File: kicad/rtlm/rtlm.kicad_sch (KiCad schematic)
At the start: 261 parts, among them IC1 ESP32-S3FN8, IC2 TPS25940ARVCR, IC3 PE4259, IC4 TPS2553DBVR, IC5 TLV9004IDR, IC6 TLV9004IDR, IC7 TCAN1042HGVDR, IC8 TPS2553DBVR, IC9 TLC59116IPWR, J1 USB_C_Receptacle_USB2.0_16P, J10 TEMP_2, J11 TEMP_3, J12 TEMP_4, J13 ANALOG_1, J14 ANALOG_2, J15 ANALOG_3, J16 ANALOG_4, J17 DM3AT-SF-PEJM5, J18 CAN_EXPANSION, J19 BATTERY_VOLTAGE_SENSE_LINE, J2 Conn_01x02, J3 UART_DEBUG_3V3, J4 LORA_ANT, J5 PULSE_1, J6 PULSE_2, J7 PULSE_3, J8 PULSE_4, J9 TEMP_1, Q1 DMP2035U-7, SW1 SW_Push, SW2 SW_Push, U1 TPS62130A, U10 RV-3028-C7, U2 TPS2116DRL, U3 TPD2EUSB30, U4 SX1262IMLTRT, U5 SN74LVC14ADR, U6 MCP3208-BI/SL, U7 REF3025AIDBZR, U8 AMC3330, U9 ADS1115IDGS, Y1 40MHz, Y2 TG2520SMN 32.0000M-MCGNNM3

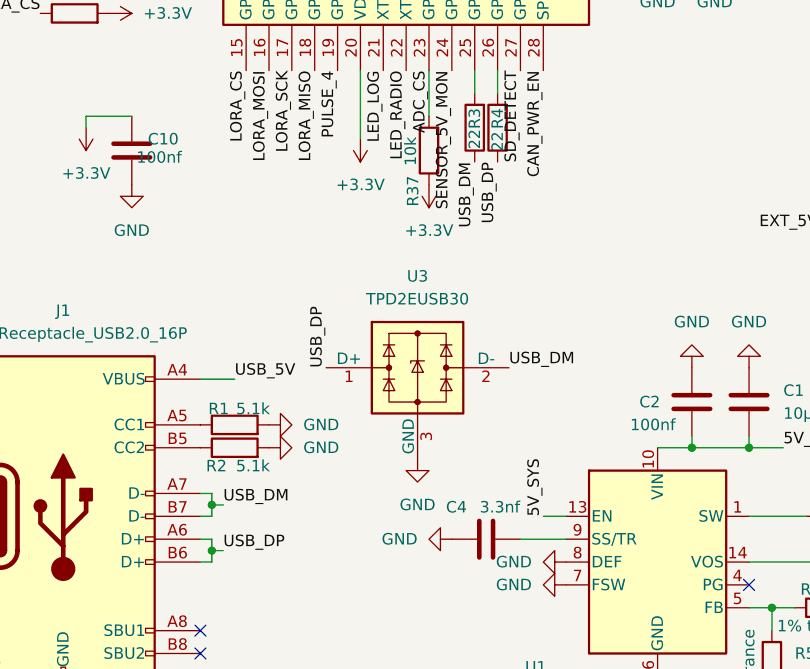
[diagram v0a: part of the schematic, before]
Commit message: feat: USB routing, thermal vias
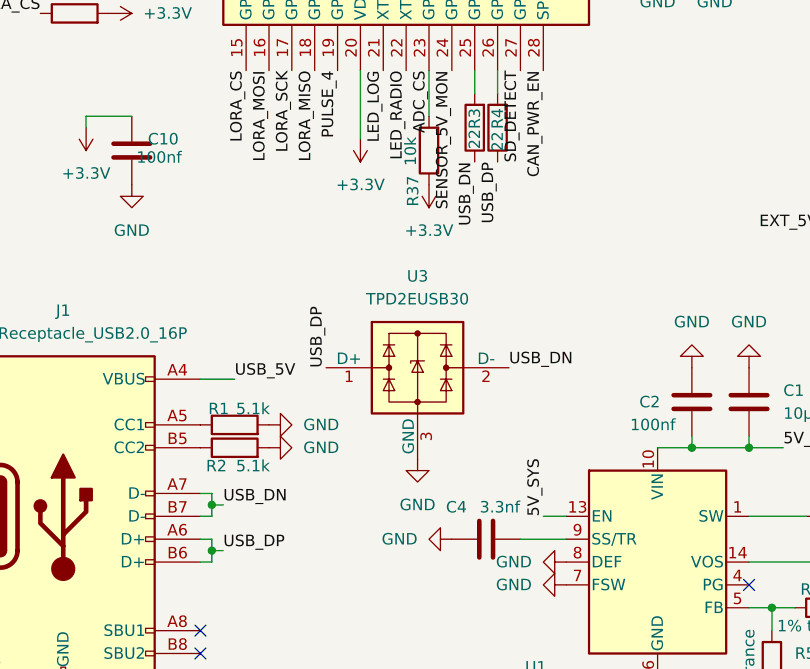
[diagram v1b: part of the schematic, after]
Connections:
- net USB_DM renamed USB_DN
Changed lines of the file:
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@@
 		)
 	)
-	(label "USB_DM"
+	(label "USB_DN"
 		(at 46.99 166.37 0)
 		(effects
@@
 		)
 	)
-	(label "USB_DM"
+	(label "USB_DN"
 		(at 74.93 128.27 270)
 		(effects
@@
 		)
 	)
-	(label "USB_DM"
+	(label "USB_DN"
 		(at 78.74 151.13 0)
 		(effects

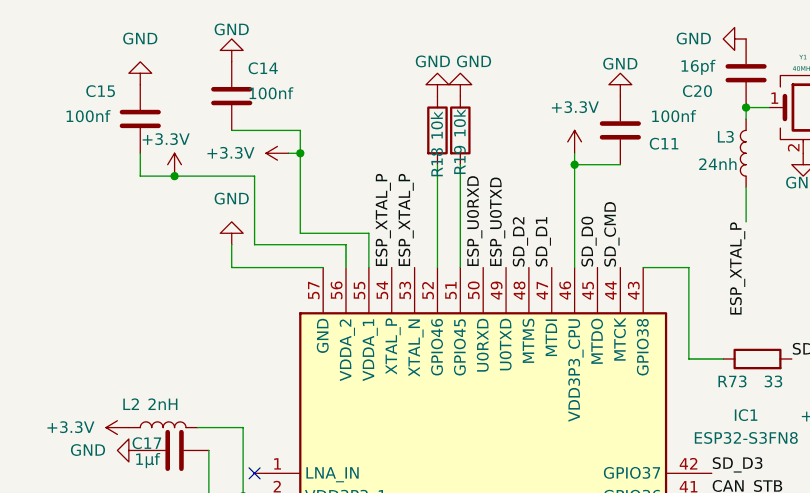
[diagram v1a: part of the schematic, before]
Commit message: feat: start IC1 routing, SD, and UART; fix misnamed UART label
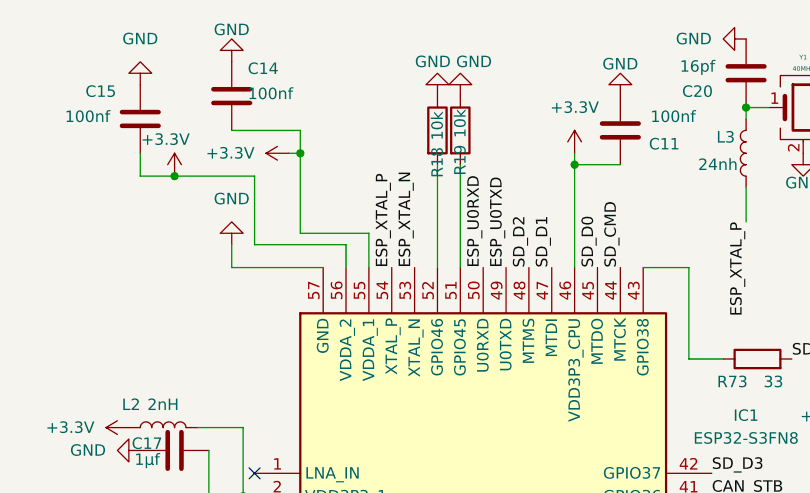
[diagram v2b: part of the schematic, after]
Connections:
- net ESP_XTAL_N: now also IC1.53 (XTAL_N)
- net ESP_XTAL_P: no longer IC1.53 (XTAL_N)
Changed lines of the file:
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@@
 		)
 	)
-	(label "ESP_XTAL_P"
+	(label "ESP_XTAL_N"
 		(at 59.69 39.37 90)
 		(effects

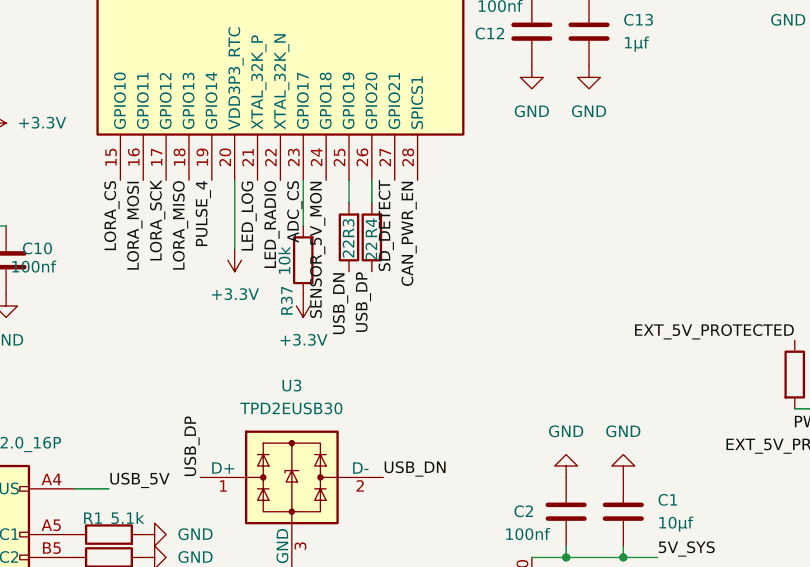
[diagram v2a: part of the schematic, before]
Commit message: feat: fix usb class and re-tune length
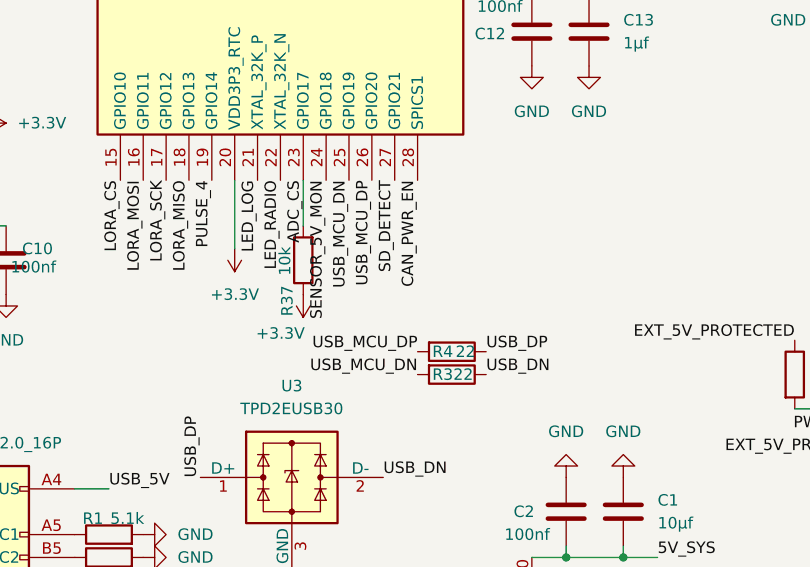
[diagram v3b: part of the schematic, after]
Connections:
- net USB_MCU_DN: now reaches IC1.25 (GPIO19), R3.2
- net USB_MCU_DP: now reaches IC1.26 (GPIO20), R4.2
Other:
- moved on the sheet: R3, R4
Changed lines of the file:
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@@
 	(wire
 		(pts
-			(xy 74.93 120.65) (xy 74.93 118.11)
-		)
-		(stroke
-			(width 0)
-			(type default)
-		)
-	)
-	(wire
-		(pts
 			(xy 39.37 295.91) (xy 39.37 293.37)
 		)
@@
 	(wire
 		(pts
-			(xy 77.47 120.65) (xy 77.47 118.11)
-		)
-		(stroke
-			(width 0)
-			(type default)
-		)
-	)
-	(wire
-		(pts
 			(xy 53.34 425.45) (xy 54.61 425.45)
 		)
@@
 		)
 	)
+	(label "USB_MCU_DN"
+		(at 82.55 139.7 180)
+		(effects
+			(font
+				(size 1.27 1.27)
+			)
+			(justify right bottom)
+		)
+	)
 	(label "ANALOG2_RAW"
 		(at 176.53 289.56 180)
@@
 		)
 	)
+	(label "USB_MCU_DN"
+		(at 74.93 118.11 270)
+		(effects
+			(font
+				(size 1.27 1.27)
+			)
+			(justify right bottom)
+		)
+	)
 	(label "LORA_BUSY"
 		(at 41.91 85.09 180)
@@
 	)
 	(label "USB_DP"
-		(at 77.47 128.27 270)
+		(at 90.17 137.16 0)
 		(effects
 			(font
 				(size 1.27 1.27)
 			)
-			(justify right bottom)
+			(justify left bottom)
 		)
 	)
@@
 		)
 	)
+	(label "USB_MCU_DP"
+		(at 77.47 118.11 270)
+		(effects
+			(font
+				(size 1.27 1.27)
+			)
+			(justify right bottom)
+		)
+	)
 	(label "USB_DP"
 		(at 58.42 151.13 90)
@@
 		)
 	)
+	(label "USB_MCU_DP"
+		(at 82.55 137.16 180)
+		(effects
+			(font
+				(size 1.27 1.27)
+			)
+			(justify right bottom)
+		)
+	)
 	(label "ADC_VREF_2V5"
 		(at 199.39 365.76 180)
@@
 	)
 	(label "USB_DN"
-		(at 74.93 128.27 270)
+		(at 90.17 139.7 0)
 		(effects
 			(font
 				(size 1.27 1.27)
 			)
-			(justify right bottom)
+			(justify left bottom)
 		)
 	)
@@
 	(symbol
 		(lib_id "Device:R")
-		(at 77.47 124.46 180)
+		(at 86.36 137.16 270)
 		(unit 1)
 		(body_style 1)
@@
 		(dnp no)
 		(property "Reference" "R4"
-			(at 77.47 123.444 90)
+			(at 85.344 137.16 90)
 			(show_name no)
 			(do_not_autoplace no)
@@
 		)
 		(property "Value" "22"
-			(at 77.47 125.984 90)
+			(at 87.884 137.16 90)
 			(show_name no)
 			(do_not_autoplace no)
@@
 		)
 		(property "Footprint" "Resistor_SMD:R_0603_1608Metric"
-			(at 79.248 124.46 90)
+			(at 86.36 135.382 90)
 			(hide yes)
 			(show_name no)
@@
 		)
 		(property "Datasheet" ""
-			(at 77.47 124.46 0)
+			(at 86.36 137.16 0)
 			(hide yes)
 			(show_name no)
@@
 		)
 		(property "Description" "Resistor"
-			(at 77.47 124.46 0)
+			(at 86.36 137.16 0)
 			(hide yes)
 			(show_name no)
@@
 		(in_pos_files yes)
 		(dnp no)
-		(fields_autoplaced yes)
 		(property "Reference" "#PWR0125"
 			(at 69.85 127 0)
@@
 		)
 		(property "Value" "+3.3V"
-			(at 69.85 135.89 0)
+			(at 67.31 135.128 0)
 			(show_name no)
 			(do_not_autoplace no)
@@
 	(symbol
 		(lib_id "Device:R")
-		(at 74.93 124.46 180)
+		(at 86.36 139.7 270)
 		(unit 1)
 		(body_style 1)
@@
 		(dnp no)
 		(property "Reference" "R3"
-			(at 74.93 123.444 90)
+			(at 85.344 139.7 90)
 			(show_name no)
 			(do_not_autoplace no)
@@
 		)
 		(property "Value" "22"
-			(at 74.93 125.73 90)
+			(at 87.63 139.7 90)
 			(show_name no)
 			(do_not_autoplace no)
@@
 		)
 		(property "Footprint" "Resistor_SMD:R_0603_1608Metric"
-			(at 76.708 124.46 90)
+			(at 86.36 137.922 90)
 			(hide yes)
 			(show_name no)
@@
 		)
 		(property "Datasheet" ""
-			(at 74.93 124.46 0)
+			(at 86.36 139.7 0)
 			(hide yes)
 			(show_name no)
@@
 		)
 		(property "Description" "Resistor"
-			(at 74.93 124.46 0)
+			(at 86.36 139.7 0)
 			(hide yes)
 			(show_name no)

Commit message: feat: power wiring around IC1
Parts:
- added C80: 10uF, Capacitor_SMD:C_0805_2012Metric, symbol Device:C
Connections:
- net GND: now also C80.1
- net at C17.2, IC1.2 (VDD3P3_1), IC1.3 (VDD3P3_2)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: now also C80.2
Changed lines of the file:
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@@
 		)
 	)
-	(wire
-		(pts
-			(xy 36.83 59.69) (xy 36.83 67.31)
-		)
-		(stroke
-			(width 0)
-			(type default)
-		)
-	)
+	(wire (pts (xy 36.83 59.69) (xy 36.83 64.77)) (stroke (width 0) (type default)))
+	(wire (pts (xy 36.83 64.77) (xy 36.83 67.31)) (stroke (width 0) (type default)))
 	(wire
 		(pts
@@
 	(symbol
 		(lib_id "power:GND")
-		(at 29.21 59.69 270)
+		(at 25.4 59.69 270)
 		(unit 1)
 		(body_style 1)
@@
 		(fields_autoplaced yes)
 		(property "Reference" "#PWR045"
-			(at 22.86 59.69 0)
+			(at 19.05 59.69 0)
 			(hide yes)
 			(show_name no)
@@
 		)
 		(property "Value" "GND"
-			(at 25.4 59.6899 90)
+			(at 21.59 59.6899 90)
 			(show_name no)
 			(do_not_autoplace no)
@@
 		)
 		(property "Footprint" ""
-			(at 29.21 59.69 0)
+			(at 25.4 59.69 0)
 			(hide yes)
 			(show_name no)
@@
 		)
 		(property "Datasheet" ""
-			(at 29.21 59.69 0)
+			(at 25.4 59.69 0)
 			(hide yes)
 			(show_name no)
@@
 		)
 		(property "Description" "Power symbol creates a global label with name \"GND\" , ground"
-			(at 29.21 59.69 0)
+			(at 25.4 59.69 0)
 			(hide yes)
 			(show_name no)
@@
 	)
 	(embedded_fonts no)
+	(symbol
+		(lib_id "Device:C")
+		(at 33.02 64.77 90)
+		(unit 1)
+		(body_style 1)
+		(exclude_from_sim no)
+		(in_bom yes)
+		(on_board yes)
+		(in_pos_files yes)
+		(dnp no)
+		(property "Reference" "C80"
+			(at 29.972 64.008 90)
+			(show_name no)
+			(do_not_autoplace no)
+			(effects
+				(font
+					(size 1.27 1.27)
+				)
+			)
+		)
+		(property "Value" "10uF"
+			(at 29.972 65.786 90)
+			(show_name no)
+			(do_not_autoplace no)
+			(effects
+				(font
+					(size 1.27 1.27)
+				)
+			)
+		)
+		(property "Footprint" "Capacitor_SMD:C_0805_2012Metric"
+			(at 36.83 63.8048 0)
+			(hide yes)
+			(show_name no)
+			(do_not_autoplace no)
+			(effects
+				(font
+					(size 1.27 1.27)
+				)
+			)
+		)
+		(property "Datasheet" ""
+			(at 33.02 64.77 0)
+			(hide yes)
+			(show_name no)
+			(do_not_autoplace no)
+			(effects
+				(font
+					(size 1.27 1.27)
+				)
+			)
+		)
+		(property "Description" "VDD3P3 bulk decoupling after L2; 10uF 10V X7R +/-10%; verify DC-bias capacitance"
+			(at 33.02 64.77 0)
+			(hide yes)
+			(show_name no)
+			(do_not_autoplace no)
+			(effects
+				(font
+					(size 1.27 1.27)
+				)
+			)
+		)
+		(pin "2"
+		)
+		(pin "1"
+		)
+		(instances
+			(project "rtlm"
+				(path "/18642f86-b1da-4982-a59b-b3bbb269065a"
+					(reference "C80")
+					(unit 1)
+				)
+			)
+		)
+	)
+	(wire (pts (xy 29.21 59.69) (xy 25.4 59.69)) (stroke (width 0) (type default)))
+	(wire (pts (xy 25.4 59.69) (xy 25.4 64.77)) (stroke (width 0) (type default)))
+	(wire (pts (xy 25.4 64.77) (xy 29.21 64.77)) (stroke (width 0) (type default)))
+	(junction (at 36.83 64.77) (diameter 0) (color 0 0 0 0))
 )

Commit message: feat: add voltage sense fuse and route sense upper half
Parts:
- added F1: 160mA T 250VDC, SamacSys_Parts:UMT-H, symbol Device:Fuse
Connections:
- net PACK_POS: now also F1.1; no longer R82.1
- new net PACK_POS_FUSED: F1.2, R82.1
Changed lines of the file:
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@@
 	)
 	(junction
+		(at 36.83 64.77)
+		(diameter 0)
+		(color 0 0 0 0)
+	)
+	(junction
 		(at 580.39 72.39)
 		(diameter 0)
@@
 	(wire
 		(pts
+			(xy 36.83 59.69) (xy 36.83 64.77)
+		)
+		(stroke
+			(width 0)
+			(type default)
+		)
+	)
+	(wire
+		(pts
 			(xy 95.25 160.02) (xy 99.06 160.02)
 		)
@@
 	(wire
 		(pts
+			(xy 25.4 64.77) (xy 29.21 64.77)
+		)
+		(stroke
+			(width 0)
+			(type default)
+		)
+	)
+	(wire
+		(pts
 			(xy 92.71 95.25) (xy 95.25 95.25)
 		)
@@
 	(wire
 		(pts
+			(xy 598.17 138.43) (xy 605.79 138.43)
+		)
+		(stroke
+			(width 0)
+			(type default)
+		)
+	)
+	(wire
+		(pts
 			(xy 308.61 208.28) (xy 308.61 210.82)
 		)
@@
 		)
 	)
-	(wire (pts (xy 36.83 59.69) (xy 36.83 64.77)) (stroke (width 0) (type default)))
-	(wire (pts (xy 36.83 64.77) (xy 36.83 67.31)) (stroke (width 0) (type default)))
 	(wire
 		(pts
@@
 	(wire
 		(pts
+			(xy 25.4 59.69) (xy 25.4 64.77)
+		)
+		(stroke
+			(width 0)
+			(type default)
+		)
+	)
+	(wire
+		(pts
 			(xy 44.45 170.18) (xy 45.72 170.18)
 		)
@@
 	(wire
 		(pts
+			(xy 29.21 59.69) (xy 25.4 59.69)
+		)
+		(stroke
+			(width 0)
+			(type default)
+		)
+	)
+	(wire
+		(pts
 			(xy 137.16 289.56) (xy 139.7 289.56)
 		)
@@
 	(wire
 		(pts
+			(xy 36.83 64.77) (xy 36.83 67.31)
+		)
+		(stroke
+			(width 0)
+			(type default)
+		)
+	)
+	(wire
+		(pts
 			(xy 29.21 300.99) (xy 40.64 300.99)
 		)
@@
 		)
 	)
+	(label "PACK_POS_FUSED"
+		(at 600.71 138.43 90)
+		(effects
+			(font
+				(size 1 1)
+			)
+			(justify left bottom)
+		)
+	)
 	(label "TEMP3_ADC"
 		(at 68.58 316.23 270)
@@
 	)
 	(label "PACK_POS"
-		(at 605.79 138.43 180)
+		(at 590.55 138.43 180)
 		(effects
 			(font
@@
 	)
 	(symbol
+		(lib_id "Device:C")
+		(at 33.02 64.77 90)
+		(unit 1)
+		(body_style 1)
+		(exclude_from_sim no)
+		(in_bom yes)
+		(on_board yes)
+		(in_pos_files yes)
+		(dnp no)
+		(property "Reference" "C80"
+			(at 29.972 64.008 90)
+			(show_name no)
+			(do_not_autoplace no)
+			(effects
+				(font
+					(size 1.27 1.27)
+				)
+			)
+		)
+		(property "Value" "10uF"
+			(at 29.972 65.786 90)
+			(show_name no)
+			(do_not_autoplace no)
+			(effects
+				(font
+					(size 1.27 1.27)
+				)
+			)
+		)
+		(property "Footprint" "Capacitor_SMD:C_0805_2012Metric"
+			(at 36.83 63.8048 0)
+			(hide yes)
+			(show_name no)
+			(do_not_autoplace no)
+			(effects
+				(font
+					(size 1.27 1.27)
+				)
+			)
+		)
+		(property "Datasheet" ""
+			(at 33.02 64.77 0)
+			(hide yes)
+			(show_name no)
+			(do_not_autoplace no)
+			(effects
+				(font
+					(size 1.27 1.27)
+				)
+			)
+		)
+		(property "Description" "VDD3P3 bulk decoupling after L2; 10uF 10V X7R +/-10%; verify DC-bias capacitance"
+			(at 33.02 64.77 0)
+			(hide yes)
+			(show_name no)
+			(do_not_autoplace no)
+			(effects
+				(font
+					(size 1.27 1.27)
+				)
+			)
+		)
+		(pin "2"
+		)
+		(pin "1"
+		)
+		(instances
+			(project "rtlm"
+				(path "/18642f86-b1da-4982-a59b-b3bbb269065a"
+					(reference "C80")
+					(unit 1)
+				)
+			)
+		)
+	)
+	(symbol
 		(lib_id "power:+3.3V")
 		(at 204.47 207.01 180)
@@
 	)
 	(symbol
+		(lib_id "Device:Fuse")
+		(at 594.36 138.43 90)
+		(unit 1)
+		(body_style 1)
+		(exclude_from_sim no)
+		(in_bom yes)
+		(on_board yes)
+		(in_pos_files yes)
+		(dnp no)
+		(property "Reference" "F1"
+			(at 594.36 135.89 90)
+			(show_name no)
+			(do_not_autoplace no)
+			(effects
+				(font
+					(size 1.27 1.27)
+				)
+			)
+		)
+		(property "Value" "160mA T 250VDC"
+			(at 594.36 142.24 90)
+			(show_name no)
+			(do_not_autoplace no)
+			(effects
+				(font
+					(size 1.27 1.27)
+				)
+			)
+		)
+		(property "Footprint" "SamacSys_Parts:UMT-H"
+			(at 594.36 140.208 90)
+			(hide yes)
+			(show_name no)
+			(do_not_autoplace no)
+			(effects
+				(font
+					(size 1.27 1.27)
+				)
+			)
+		)
+		(property "Datasheet" "https://www.schurter.com/fr/datasheet/typ_UMT-H.pdf"
+			(at 594.36 138.43 0)
+			(hide yes)
+			(show_name no)
+			(do_not_autoplace no)
+			(effects
+				(font
+					(size 1.27 1.27)
+				)
+			)
+		)
+		(property "Description" "SCHURTER 3403.0266.23; 1500A DC breaking capacity"
+			(at 593.852 134.366 90)
+			(hide yes)
+			(show_name no)
+			(do_not_autoplace no)
+			(effects
+				(font
+					(size 1.27 1.27)
+				)
+			)
+		)
+		(property "Manufacturer" "SCHURTER"
+			(at 594.36 138.43 0)
+			(hide yes)
+			(show_name no)
+			(do_not_autoplace no)
+			(effects
+				(font
+					(size 1.27 1.27)
+				)
+			)
+		)
+		(property "MPN" "3403.0266.23"
+			(at 594.36 138.43 0)
+			(hide yes)
+			(show_name no)
+			(do_not_autoplace no)
+			(effects
+				(font
+					(size 1.27 1.27)
+				)
+			)
+		)
+		(pin "1"
+		)
+		(pin "2"
+		)
+		(instances
+			(project "rtlm"
+				(path "/18642f86-b1da-4982-a59b-b3bbb269065a"
+					(reference "F1")
+					(unit 1)
+				)
+			)
+		)
+	)
+	(symbol
 		(lib_id "power:+3.3V")
 		(at 317.5 264.16 90)
@@
 	)
 	(embedded_fonts no)
-	(symbol
-		(lib_id "Device:C")
-		(at 33.02 64.77 90)
-		(unit 1)
-		(body_style 1)
-		(exclude_from_sim no)
-		(in_bom yes)
-		(on_board yes)
-		(in_pos_files yes)
-		(dnp no)
-		(property "Reference" "C80"
-			(at 29.972 64.008 90)
-			(show_name no)
-			(do_not_autoplace no)
-			(effects
-				(font
-					(size 1.27 1.27)
-				)
-			)
-		)
-		(property "Value" "10uF"
-			(at 29.972 65.786 90)
-			(show_name no)
-			(do_not_autoplace no)
-			(effects
-				(font
-					(size 1.27 1.27)
-				)
-			)
-		)
-		(property "Footprint" "Capacitor_SMD:C_0805_2012Metric"
-			(at 36.83 63.8048 0)
-			(hide yes)
-			(show_name no)
-			(do_not_autoplace no)
-			(effects
-				(font
-					(size 1.27 1.27)
-				)
-			)
-		)
-		(property "Datasheet" ""
-			(at 33.02 64.77 0)
-			(hide yes)
-			(show_name no)
-			(do_not_autoplace no)
-			(effects
-				(font
-					(size 1.27 1.27)
-				)
-			)
-		)
-		(property "Description" "VDD3P3 bulk decoupling after L2; 10uF 10V X7R +/-10%; verify DC-bias capacitance"
-			(at 33.02 64.77 0)
-			(hide yes)
-			(show_name no)
-			(do_not_autoplace no)
-			(effects
-				(font
-					(size 1.27 1.27)
-				)
-			)
-		)
-		(pin "2"
-		)
-		(pin "1"
-		)
-		(instances
-			(project "rtlm"
-				(path "/18642f86-b1da-4982-a59b-b3bbb269065a"
-					(reference "C80")
-					(unit 1)
-				)
-			)
-		)
-	)
-	(wire (pts (xy 29.21 59.69) (xy 25.4 59.69)) (stroke (width 0) (type default)))
-	(wire (pts (xy 25.4 59.69) (xy 25.4 64.77)) (stroke (width 0) (type default)))
-	(wire (pts (xy 25.4 64.77) (xy 29.21 64.77)) (stroke (width 0) (type default)))
-	(junction (at 36.83 64.77) (diameter 0) (color 0 0 0 0))
 )

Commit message: feat: full prelim routing
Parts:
- added C81: 10uF, Capacitor_SMD:C_0805_2012Metric, symbol Device:C
- R11: value 59k -> 42.2k
- R34: value 133k -> 52.3k
- R81: value 133k -> 88.7k
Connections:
- net 5V_SYS: now also C81.1
- net GND: now also C81.2
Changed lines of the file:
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@@
 			)
 		)
-		(property "Value" "59k"
+		(property "Value" "42.2k"
 			(at 189.23 39.3699 0)
 			(show_name no)
@@
 			)
 		)
-		(property "Datasheet" "http://www.ti.com/lit/gpn/sn74HC14"
+		(property "Datasheet" "https://www.ti.com/lit/ds/symlink/sn74lvc14a.pdf"
 			(at 62.23 425.45 0)
 			(hide yes)
@@
 			)
 		)
-		(property "Description" "Hex inverter schmitt trigger"
+		(property "Description" "SN74LVC14A hex Schmitt-trigger inverter; 1.65-3.6V supply; 5.5V-tolerant inputs"
 			(at 62.23 425.45 0)
 			(hide yes)
@@
 			)
 		)
-		(property "Description" "Espressif Systems [ENGINEERING SAMPLES]SMD IC , Dual-Core MCU, Wi-Fi 2.4G & BLE 5.0 combo, 8 MB Octal SPI PSRAM"
+		(property "Description" "ESP32-S3FN8; 8 MB in-package Quad SPI flash; no in-package PSRAM"
 			(at 41.91 62.23 0)
 			(hide yes)
@@
 			)
 		)
-		(property "Value" "133k"
+		(property "Value" "88.7k"
 			(at 475.488 234.442 90)
 			(show_name no)
@@
 			)
 		)
-		(property "Value" "133k"
+		(property "Value" "52.3k"
 			(at 203.962 196.85 90)
 			(show_name no)
@@
 	)
 	(embedded_fonts no)
+	(symbol
+		(lib_id "Device:C")
+		(at 515.62 241.3 90)
+		(unit 1)
+		(body_style 1)
+		(exclude_from_sim no)
+		(in_bom yes)
+		(on_board yes)
+		(in_pos_files yes)
+		(dnp no)
+		(property "Reference" "C81"
+			(at 513.334 237.744 90)
+			(show_name no)
+			(do_not_autoplace no)
+			(effects
+				(font
+					(size 1.27 1.27)
+				)
+			)
+		)
+		(property "Value" "10uF"
+			(at 518.414 237.744 90)
+			(show_name no)
+			(do_not_autoplace no)
+			(effects
+				(font
+					(size 1.27 1.27)
+				)
+			)
+		)
+		(property "Footprint" "Capacitor_SMD:C_0805_2012Metric"
+			(at 519.43 240.335 0)
+			(hide yes)
+			(show_name no)
+			(do_not_autoplace no)
+			(effects
+				(font
+					(size 1.27 1.27)
+				)
+			)
+		)
+		(property "Datasheet" ""
+			(at 515.62 241.3 0)
+			(hide yes)
+			(show_name no)
+			(do_not_autoplace no)
+			(effects
+				(font
+					(size 1.27 1.27)
+				)
+			)
+		)
+		(property "Description" "CAN VCC local bulk; 10uF 16V X7R 0805; select >=4.7uF effective at 5V over tolerance and temperature"
+			(at 515.62 241.3 0)
+			(hide yes)
+			(show_name no)
+			(do_not_autoplace no)
+			(effects
+				(font
+					(size 1.27 1.27)
+				)
+			)
+		)
+		(pin "1"
+		)
+		(pin "2"
+		)
+		(instances
+			(project "rtlm"
+				(path "/18642f86-b1da-4982-a59b-b3bbb269065a"
+					(reference "C81")
+					(unit 1)
+				)
+			)
+		)
+	)
+	(label "5V_SYS" (at 511.81 241.3 0) (effects (font (size 1.27 1.27)) (justify right bottom)))
+	(label "GND" (at 519.43 241.3 0) (effects (font (size 1.27 1.27)) (justify left bottom)))
 )
